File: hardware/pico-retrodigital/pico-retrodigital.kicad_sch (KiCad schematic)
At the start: 69 parts, among them J1 Conn_02x05_Top_Bottom, J3 Conn_01x14, J4 Conn_01x02_Pin, J5 USB_C_Plug_USB2.0, SW1 BOOT, SW2 RES, U1 SN74LVC1G17DBVR, U2 SN74LVC1G17DBVR, U3 RP2354B, U4 SN74LVC245APW, U5 SN74LVC245APW, U6 SN74LVC245APW, U8 ME6217C33M5G, Y1 ABM8-272-T3

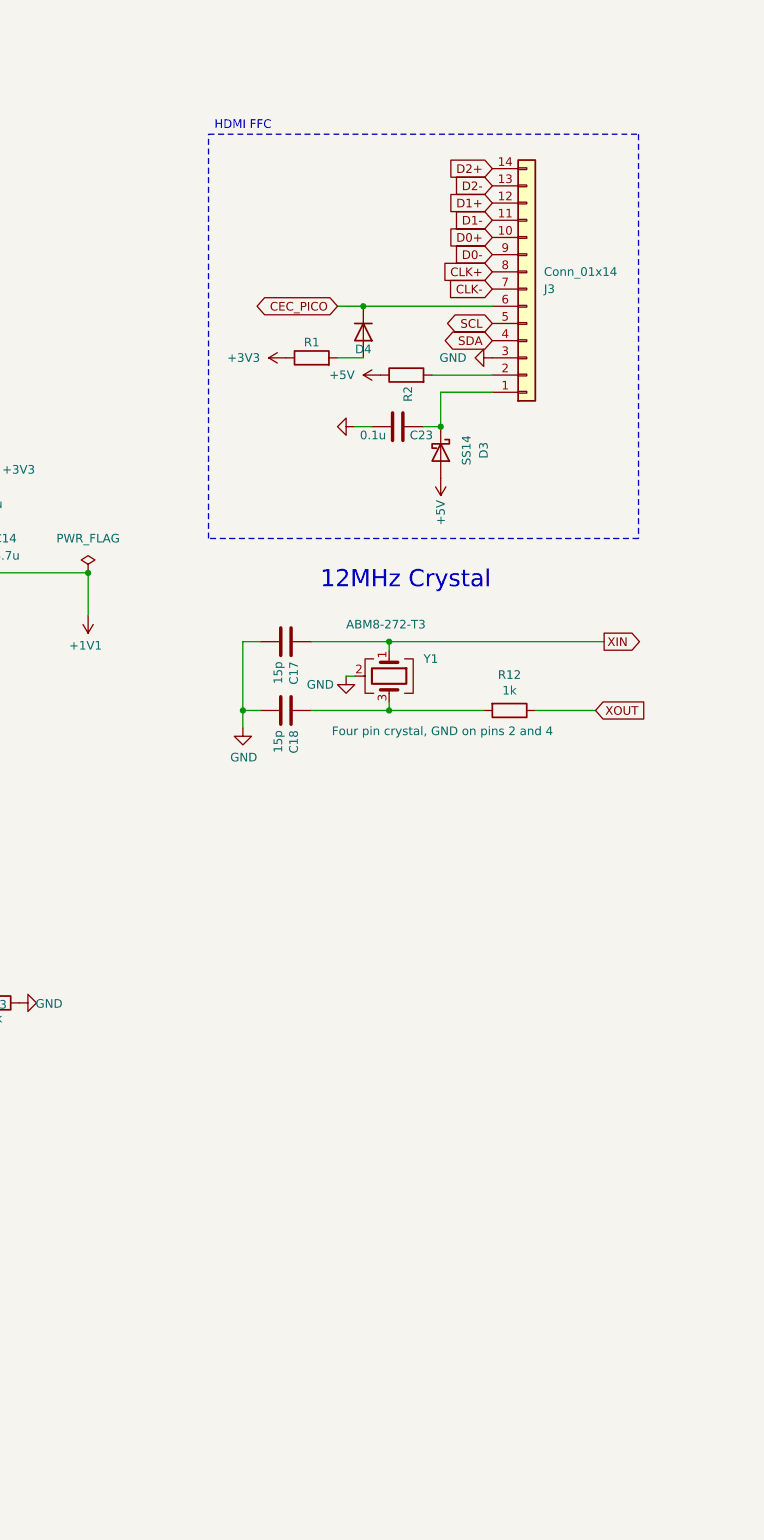
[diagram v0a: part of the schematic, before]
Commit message: Two HDMI out connectors
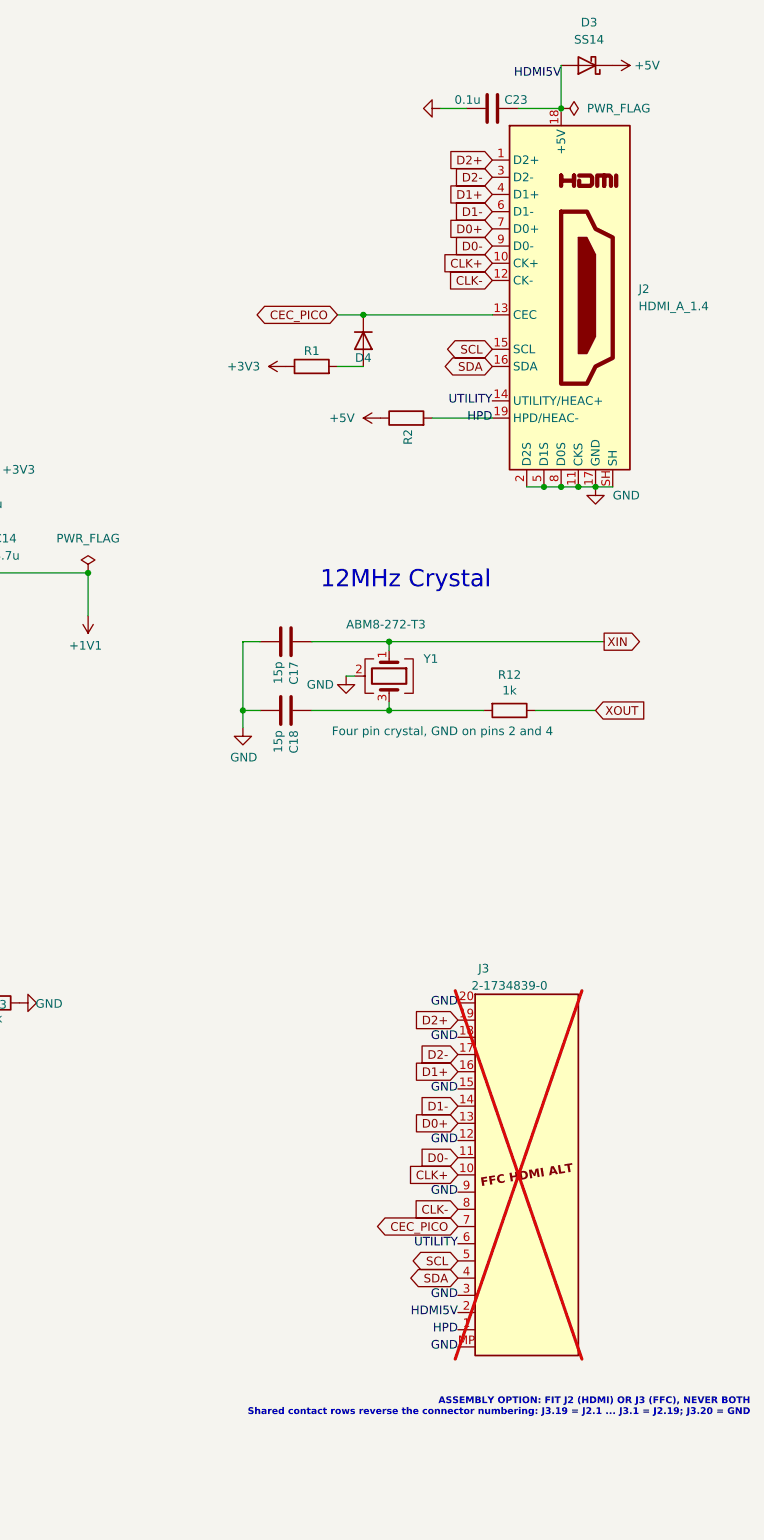
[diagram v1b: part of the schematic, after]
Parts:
- removed J3: Conn_01x14, Connector_FFC-FPC:TE_1-1734839-4_1x14-1MP_P0.5mm_Horizontal, symbol Connector_Generic:Conn_01x14
- added J2: HDMI_A_1.4, Connector_Video:HDMI_A_Molex_208658-1001_Horizontal, symbol Connector:HDMI_A_1.4
- added J3: 2-1734839-0, Connector_FFC-FPC:TE_2-1734839-0_1x20-1MP_P0.5mm_Horizontal, symbol pico-retrodigital:HDMI_FFC_20_Alternate
- C19: footprint Capacitor_THT:CP_Radial_D4.0mm_P2.00mm -> Capacitor_SMD:C_Elec_5x5.4
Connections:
- net +5V: now also D3.1 (K); no longer D3.2 (A)
- net CEC_PICO: now also J2.13 (CEC), J3.7 (CEC)
- net CLK+: now also J2.10 (CK+), J3.10 (CLK+)
- net CLK-: now also J2.12 (CK-), J3.8 (CLK-)
- net D0+: now also J2.7 (D0+), J3.13 (D0+)
- net D0-: now also J2.9 (D0-), J3.11 (D0-)
- net D1+: now also J2.4 (D1+), J3.16 (D1+)
- net D1-: now also J2.6 (D1-), J3.14 (D1-)
- net D2+: now also J2.1 (D2+), J3.19 (D2+)
- net D2-: now also J2.3 (D2-), J3.17 (D2-)
- net GND: now also J2.11 (CKS), J2.17 (GND), J2.2 (D2S), J2.5 (D1S), J2.8 (D0S), J2.SH, J3.12 (GND), J3.15 (GND), J3.18 (GND), J3.20 (GND), J3.3 (GND), J3.9 (GND), J3.MP (SHIELD)
- net SCL: now also J2.15 (SCL), J3.5 (SCL)
- net SDA: now also J2.16 (SDA), J3.4 (SDA)
- net HDMI5V: now reaches C23.1
- net HDMI5V: now also D3.2 (A), J2.18 (+5V), J3.2 (+5V); no longer D3.1 (K)
- net HPD: now reaches R2.2
- net HPD: now also J2.19 (HPD/HEAC-), J3.1 (HPD)
- new net UTILITY: J2.14 (UTILITY/HEAC+), J3.6 (UTILITY)
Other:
- note added: "ASSEMBLY OPTION: FIT J2 (HDMI) OR J3 (FFC), NEVER BOTH Shared contact rows reverse the connector numbering: J3.19 = J2.1 ... J3.1 = J2.19; J3.20 = GND"
- note removed: "HDMI FFC"
- moved on the sheet: D4, R1

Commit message: Source everything from JLC: LCSC part fill, connector swaps, fab export fixes
- Fill LCSC/MPN fields across the BOM (fill_lcsc script + curated picks);
  replace generic values with specific parts (diodes, LEDs, polyfuse,
  ferrite bead, switches)
- C19: SMD electrolytic -> 47uF 1206 MLCC (keeps Economic assembly)
- J1/J3: TE 1734839 FFC -> LCSC-stocked double-sided-contact parts
  (AFC24-S32FIA-00 / Molex 5034802000), project-local footprints
- J5: GCT USB4105 -> HRO TYPE-C-31-M-12 (C165948)
- D3/D4: SS14 -> true 0603 Schottky (CD0603-B0340R)
- Fabrication Toolkit rotation offsets for J2/U3; J3/J4 DNP and
  excluded from BOM/CPL; remove duplicate C5 footprint
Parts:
- C1, C11, C16, C20, C21, C22, C23, C3, C4, C5, C6, C7, C8, C9: LCSC (none) -> C1525
- C10, C12: LCSC (none) -> C15525
- C13, C15: LCSC (none) -> C23733
- C14: LCSC (none) -> C19666
- C17, C18: LCSC (none) -> C1548
- C19: footprint Capacitor_SMD:C_Elec_5x5.4 -> Capacitor_SMD:C_1206_3216Metric; LCSC (none) -> C96123; MPN (none) -> CL31A476MPHNNNE
- C2: LCSC (none) -> C14663
- C24, C25, C26: LCSC C1711 -> C1525
- D1: value D_Schottky -> DSK14; LCSC (none) -> C7502711
- D2: value D_Schottky -> DSK14; LCSC C37049 -> C7502711; MPN (none) -> DSK14
- D3, D4: value SS14 -> CD0603-B0340R; LCSC (none) -> C3759853; MPN (none) -> CD0603-B0340R
- D5: value LED -> GREEN; LCSC (none) -> C2289; MPN (none) -> KT-0603YG
- D6: value LED -> RED; LCSC (none) -> C2286; MPN (none) -> KT-0603R
- F1: value Polyfuse -> 500mA; LCSC (none) -> C883095; MPN (none) -> BSMD0603-050-6V
- FB1: value FerriteBead -> 600R@100MHz; LCSC (none) -> C85833; MPN (none) -> BLM18KG601SN1D
- J1: value Conn_02x05_Top_Bottom -> AFC24-S32FIA-00; footprint Connector_FFC-FPC:TE_3-1734839-2_1x32-1MP_P0.5mm_Horizontal -> pico-retrodigital:FPC-SMD_P0.50-32P_JS_AFC24-S32FIA-00; LCSC (none) -> C2908587; MPN (none) -> AFC24-S32FIA-00
- J2: FT Rotation Offset (none) -> 90; LCSC (none) -> C138388; MPN (none) -> HDMI-001 19PCBTP
- J3: value 2-1734839-0 -> 5034802000; footprint Connector_FFC-FPC:TE_2-1734839-0_1x20-1MP_P0.5mm_Horizontal -> pico-retrodigital:FPC-SMD_5034802000; LCSC (none) -> C234192; MPN (none) -> 5034802000; now left out of the parts list
- J4: LCSC (none) -> C263753; MPN (none) -> B02B-XASK-1(LF)(SN); now not fitted; now left out of the parts list
- J5: footprint Connector_USB:USB_C_Receptacle_GCT_USB4105-xx-A_16P_TopMnt_Horizontal -> pico-retrodigital:USB_C_Receptacle_HRO_TYPE-C-31-M-12; LCSC C963370 -> C165948; MPN (none) -> TYPE-C-31-M-12
- R1: LCSC (none) -> C25771
- R10, R3, R4, R5, R6, R7, R8, R9: LCSC (none) -> C25091
- R11, R12, R13: LCSC (none) -> C11702
- R14, R20: LCSC (none) -> C4109
- R15: LCSC (none) -> C25105
- R16, R17: LCSC (none) -> C25190
- R18, R19: LCSC (none) -> C23186
- R2: LCSC (none) -> C25804
- SW1: value BOOT -> K2-1808SN-A4SW-01; JLCPCB C92589 -> (none); LCSC (none) -> C92589
- SW2: value RES -> K2-1808SN-A4SW-01; JLCPCB C92589 -> (none); LCSC (none) -> C92589
- U1, U2: LCSC (none) -> C7836
- U3: FT Rotation Offset (none) -> -90; LCSC (none) -> C39843328
- U4, U5, U6: LCSC (none) -> C7848
- U8: LCSC (none) -> C427602
- Y1: LCSC (none) -> C20625731
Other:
- note added: "BOOT"
- note added: "RES"

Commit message: Add SW3/SW4 user buttons on GPIO4/GPIO5; 4-layer board
- Two new pushbuttons (same K2-1808SN as BOOT/RES) with 1k series
  resistors to GND, routed on In1.Cu
- Board converted to 4 copper layers, JLC7628 1.6mm stackup documented;
  inner layers are plain signal layers
- USB-C J5: FT Position Offset 1.42mm (JLC part origin vs KiCad anchor,
  measured via shell-hole alignment against JLC's own footprint)
- Restore GPIO6 no-connect marker
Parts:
- added R21, R22: 1k, Resistor_SMD:R_0402_1005Metric, symbol Device:R
- added SW3, SW4: K2-1808SN-A4SW-01, Button_Switch_SMD:SW_Push_1P1T_NO_Vertical_Wuerth_434133025816, symbol Switch:SW_Push
- J5: FT Position Offset (none) -> 0,1.42
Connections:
- net GND: now also R21.1, R22.1
- net at U3.1 (GPIO4): now also SW3.2
- net at U3.2 (GPIO5): now also SW4.2
- new net: R22.2, SW4.1
- new net: R21.2, SW3.1
- no-connect marks 20 -> 18
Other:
- note added: "MENU"
- note added: "SEL"
